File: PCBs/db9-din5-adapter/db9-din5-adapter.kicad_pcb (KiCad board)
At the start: 2 copper layers, 35.1 x 27.3 mm, 4 parts, among them J1 DB25_Plug_MountingHoles, J2 TX/RX Straight/cross, J3 DTR/RTS Straight/cross

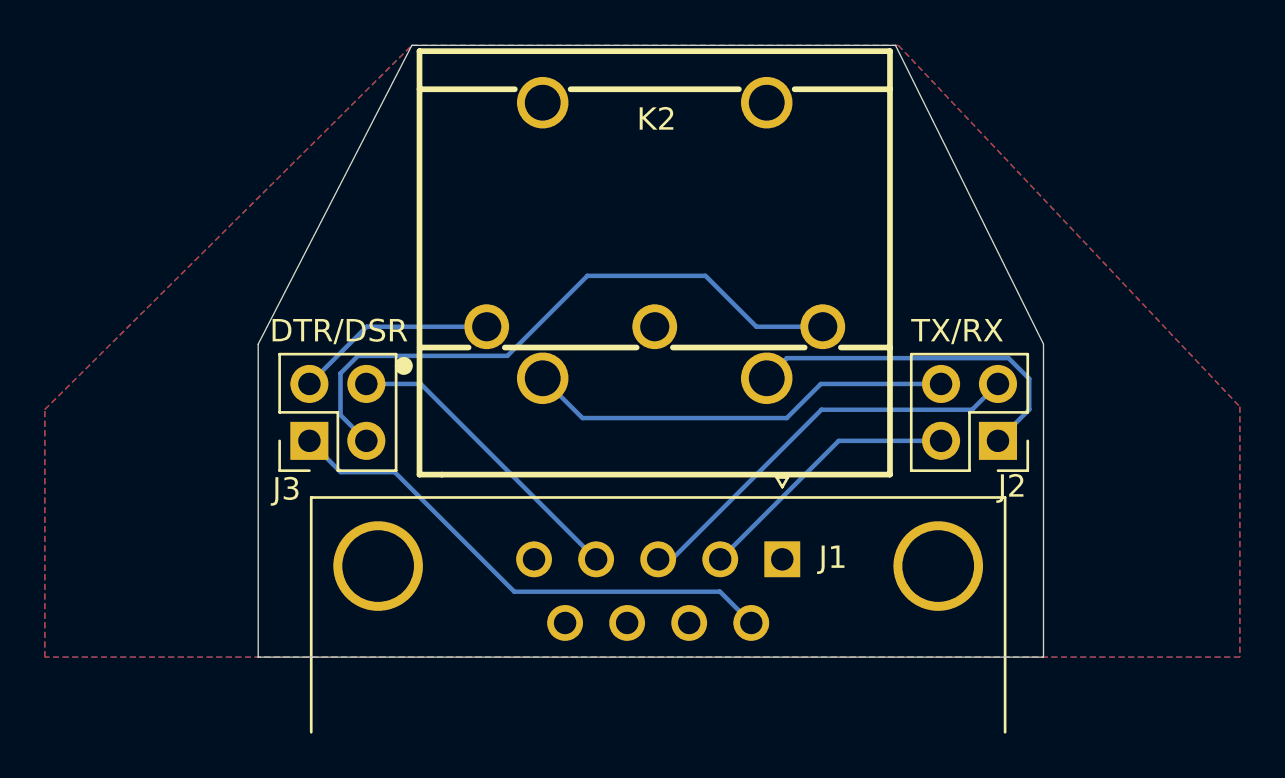
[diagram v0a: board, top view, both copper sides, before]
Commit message: Update Quicktake doc and PCBs
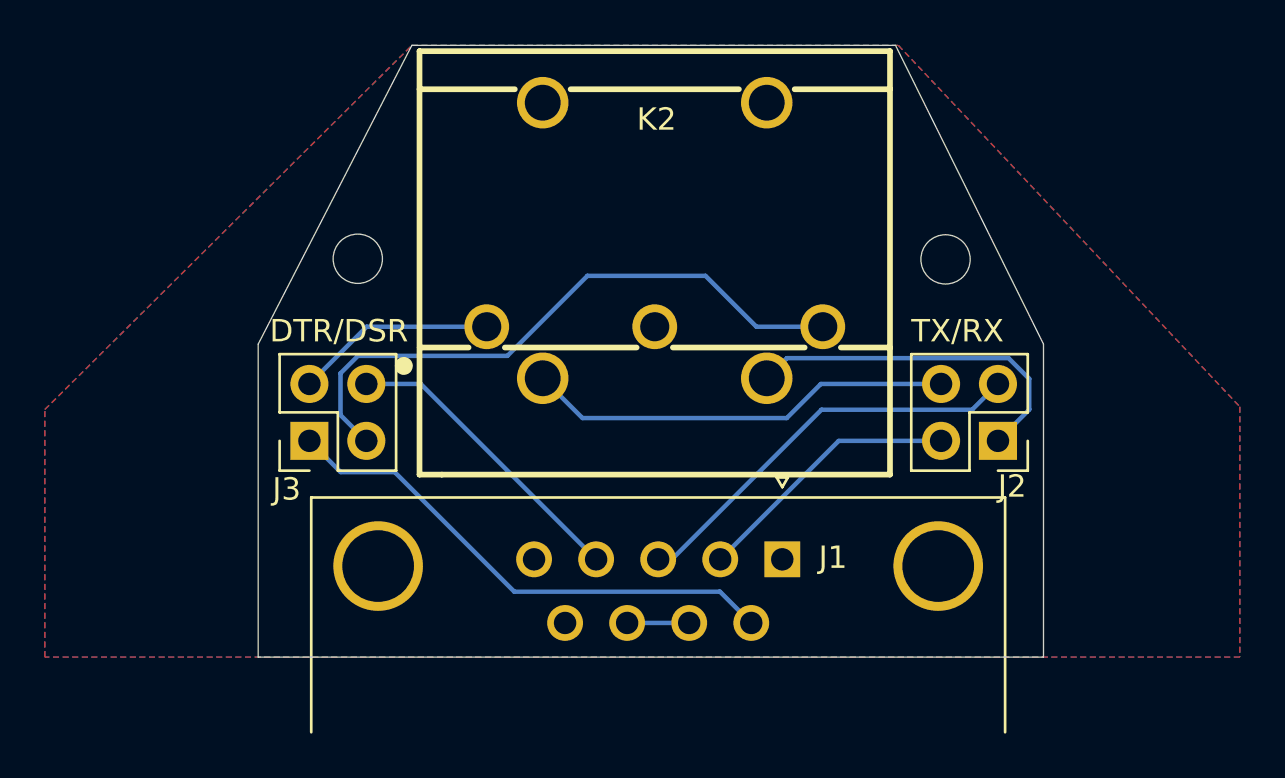
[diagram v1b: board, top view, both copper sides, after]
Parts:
- added REF**: MountingHole_2.2mm_M2, MountingHole:MountingHole_2.2mm_M2, F.Cu at (98.9, 71.2)
- added REF**: MountingHole_2.2mm_M2, MountingHole:MountingHole_2.2mm_M2, F.Cu at (125.2, 71.3)
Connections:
- J1 pad 7: unconnected-(J1-Pad7) -> Net-(J1-Pad7)
- J1 pad 8: unconnected-(J1-Pad8) -> Net-(J1-Pad7)
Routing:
- net Net-(J1-Pad7): track 0.00 -> 2.77 mm
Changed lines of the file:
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@@
 	(net 6 "unconnected-(J1-Pad9)")
 	(net 7 "DTR")
-	(net 8 "unconnected-(J1-Pad7)")
-	(net 9 "unconnected-(J1-Pad8)")
+	(net 8 "Net-(J1-Pad7)")
+	(footprint "MountingHole:MountingHole_2.2mm_M2"
+		(layer "F.Cu")
+		(at 98.933 71.247)
+		(descr "Mounting Hole 2.2mm, M2, no annular, generated by kicad-footprint-generator mountinghole.py")
+		(tags "mountinghole M2")
+		(property "Reference" "REF**"
+			(at 0 -3.15 0)
+			(layer "F.Fab")
+			(effects
+				(font
+					(size 1 1)
+					(thickness 0.15)
+				)
+			)
+		)
+		(property "Value" "MountingHole_2.2mm_M2"
+			(at 0 3.15 0)
+			(layer "F.Fab")
+			(effects
+				(font
+					(size 1 1)
+					(thickness 0.15)
+				)
+			)
+		)
+		(property "Datasheet" ""
+			(at 0 0 0)
+			(layer "F.Fab")
+			(hide yes)
+			(effects
+				(font
+					(size 1.27 1.27)
+					(thickness 0.15)
+				)
+			)
+		)
+		(property "Description" ""
+			(at 0 0 0)
+			(layer "F.Fab")
+			(hide yes)
+			(effects
+				(font
+					(size 1.27 1.27)
+					(thickness 0.15)
+				)
+			)
+		)
+		(attr board_only exclude_from_pos_files exclude_from_bom)
+		(fp_circle
+			(center 0 0)
+			(end 2.2 0)
+			(stroke
+				(width 0.15)
+				(type solid)
+			)
+			(fill no)
+			(layer "Cmts.User")
+		)
+		(fp_circle
+			(center 0 0)
+			(end 2.45 0)
+			(stroke
+				(width 0.05)
+				(type solid)
+			)
+			(fill no)
+			(layer "F.CrtYd")
+		)
+		(fp_text user "${REFERENCE}"
+			(at 0 0 0)
+			(layer "F.Fab")
+			(effects
+				(font
+					(size 1 1)
+					(thickness 0.15)
+				)
+			)
+		)
+		(pad "" np_thru_hole circle
+			(at 0 0)
+			(size 2.2 2.2)
+			(drill 2.2)
+			(layers "*.Cu" "*.Mask")
+		)
+		(embedded_fonts no)
+	)
 	(footprint "Connector_Dsub:DSUB-9_Female_Horizontal_P2.77x2.84mm_EdgePinOffset4.94mm_Housed_MountingHolesOffset7.48mm"
 		(layer "F.Cu")
@@
 			(layers "*.Cu" "*.Mask")
 			(remove_unused_layers no)
-			(net 8 "unconnected-(J1-Pad7)")
+			(net 8 "Net-(J1-Pad7)")
 			(pinfunction "7")
 			(pintype "passive")
@@
 			(layers "*.Cu" "*.Mask")
 			(remove_unused_layers no)
-			(net 9 "unconnected-(J1-Pad8)")
+			(net 8 "Net-(J1-Pad7)")
 			(pinfunction "8")
 			(pintype "passive")
@@
 			)
 		)
+	)
+	(footprint "MountingHole:MountingHole_2.2mm_M2"
+		(layer "F.Cu")
+		(at 125.168111 71.274395)
+		(descr "Mounting Hole 2.2mm, M2, no annular, generated by kicad-footprint-generator mountinghole.py")
+		(tags "mountinghole M2")
+		(property "Reference" "REF**"
+			(at 0 -3.15 0)
+			(layer "F.Fab")
+			(effects
+				(font
+					(size 1 1)
+					(thickness 0.15)
+				)
+			)
+		)
+		(property "Value" "MountingHole_2.2mm_M2"
+			(at 0 3.15 0)
+			(layer "F.Fab")
+			(effects
+				(font
+					(size 1 1)
+					(thickness 0.15)
+				)
+			)
+		)
+		(property "Datasheet" ""
+			(at 0 0 0)
+			(layer "F.Fab")
+			(hide yes)
+			(effects
+				(font
+					(size 1.27 1.27)
+					(thickness 0.15)
+				)
+			)
+		)
+		(property "Description" ""
+			(at 0 0 0)
+			(layer "F.Fab")
+			(hide yes)
+			(effects
+				(font
+					(size 1.27 1.27)
+					(thickness 0.15)
+				)
+			)
+		)
+		(attr board_only exclude_from_pos_files exclude_from_bom)
+		(fp_circle
+			(center 0 0)
+			(end 2.2 0)
+			(stroke
+				(width 0.15)
+				(type solid)
+			)
+			(fill no)
+			(layer "Cmts.User")
+		)
+		(fp_circle
+			(center 0 0)
+			(end 2.45 0)
+			(stroke
+				(width 0.05)
+				(type solid)
+			)
+			(fill no)
+			(layer "F.CrtYd")
+		)
+		(fp_text user "${REFERENCE}"
+			(at 0 0 0)
+			(layer "F.Fab")
+			(effects
+				(font
+					(size 1 1)
+					(thickness 0.15)
+				)
+			)
+		)
+		(pad "" np_thru_hole circle
+			(at 0 0)
+			(size 2.2 2.2)
+			(drill 2.2)
+			(layers "*.Cu" "*.Mask")
+		)
+		(embedded_fonts no)
 	)
 	(footprint "Connector_PinHeader_2.54mm:PinHeader_2x02_P2.54mm_Vertical"
@@
 	)
 	(gr_line
-		(start 129.54 89.027)
-		(end 129.54 75.057)
+		(start 94.488 75.057)
+		(end 101.346 61.722)
+		(stroke
+			(width 0.05)
+			(type default)
+		)
+		(layer "Edge.Cuts")
+	)
+	(gr_line
+		(start 94.488 89.027)
+		(end 94.488 75.057)
 		(stroke
 			(width 0.05)
@@
 	)
 	(gr_line
+		(start 122.936 61.722)
+		(end 101.346 61.722)
+		(stroke
+			(width 0.05)
+			(type default)
+		)
+		(layer "Edge.Cuts")
+	)
+	(gr_line
 		(start 129.54 75.057)
 		(end 122.936 61.722)
@@
 	)
 	(gr_line
-		(start 122.936 61.722)
-		(end 101.346 61.722)
+		(start 129.54 89.027)
+		(end 129.54 75.057)
 		(stroke
 			(width 0.05)
@@
 		(layer "Edge.Cuts")
 	)
-	(gr_line
-		(start 94.488 89.027)
-		(end 94.488 75.057)
-		(stroke
-			(width 0.05)
-			(type default)
-		)
-		(layer "Edge.Cuts")
-	)
-	(gr_line
-		(start 94.488 75.057)
-		(end 101.346 61.722)
-		(stroke
-			(width 0.05)
-			(type default)
-		)
-		(layer "Edge.Cuts")
+	(gr_text "DTR/DSR"
+		(at 94.996 75.057 0)
+		(layer "F.SilkS")
+		(effects
+			(font
+				(size 1 1)
+				(thickness 0.1)
+			)
+			(justify left bottom)
+		)
 	)
 	(gr_text "TX/RX"
@@
 		)
 	)
-	(gr_text "DTR/DSR"
-		(at 94.996 75.057 0)
-		(layer "F.SilkS")
+	(gr_text "Apple II serial\nDB9-DIN5 adapter"
+		(at 118.999 68.58 0)
+		(layer "B.SilkS")
 		(effects
 			(font
@@
 				(thickness 0.1)
 			)
-			(justify left bottom)
+			(justify left bottom mirror)
+		)
+	)
+	(gr_text "DB9F"
+		(at 121.92 88.011 0)
+		(layer "B.SilkS")
+		(effects
+			(font
+				(size 1 1)
+				(thickness 0.1)
+			)
+			(justify left bottom mirror)
+		)
+	)
+	(gr_text "↔ Straight\n↕ Cross-over"
+		(at 118.999 72.009 0)
+		(layer "B.SilkS")
+		(effects
+			(font
+				(size 1 1)
+				(thickness 0.125)
+			)
+			(justify left bottom mirror)
 		)
 	)
@@
 		)
 	)
-	(gr_text "DB9F"
-		(at 121.92 88.011 0)
-		(layer "B.SilkS")
-		(effects
-			(font
-				(size 1 1)
-				(thickness 0.1)
-			)
-			(justify left bottom mirror)
-		)
-	)
 	(gr_text "DTR"
 		(at 108.204 82.55 0)
@@
 		)
 	)
-	(gr_text "↔ Straight\n↕ Cross-over"
-		(at 118.999 72.009 0)
-		(layer "B.SilkS")
-		(effects
-			(font
-				(size 1 1)
-				(thickness 0.125)
-			)
-			(justify left bottom mirror)
-		)
-	)
-	(gr_text "Apple II serial\nDB9-DIN5 adapter"
-		(at 118.999 68.58 0)
-		(layer "B.SilkS")
-		(effects
-			(font
-				(size 1 1)
-				(thickness 0.1)
-			)
-			(justify left bottom mirror)
-		)
-	)
 	(segment
 		(start 126.357 77.986)
@@
 		(net 7)
 	)
+	(segment
+		(start 110.956 87.503)
+		(end 113.726 87.503)
+		(width 0.2)
+		(layer "B.Cu")
+		(net 8)
+	)
 	(zone
